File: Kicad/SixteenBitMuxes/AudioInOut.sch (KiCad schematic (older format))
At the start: 3 parts, among them J1 Audio In/Out JST XH, U25 CD4053B

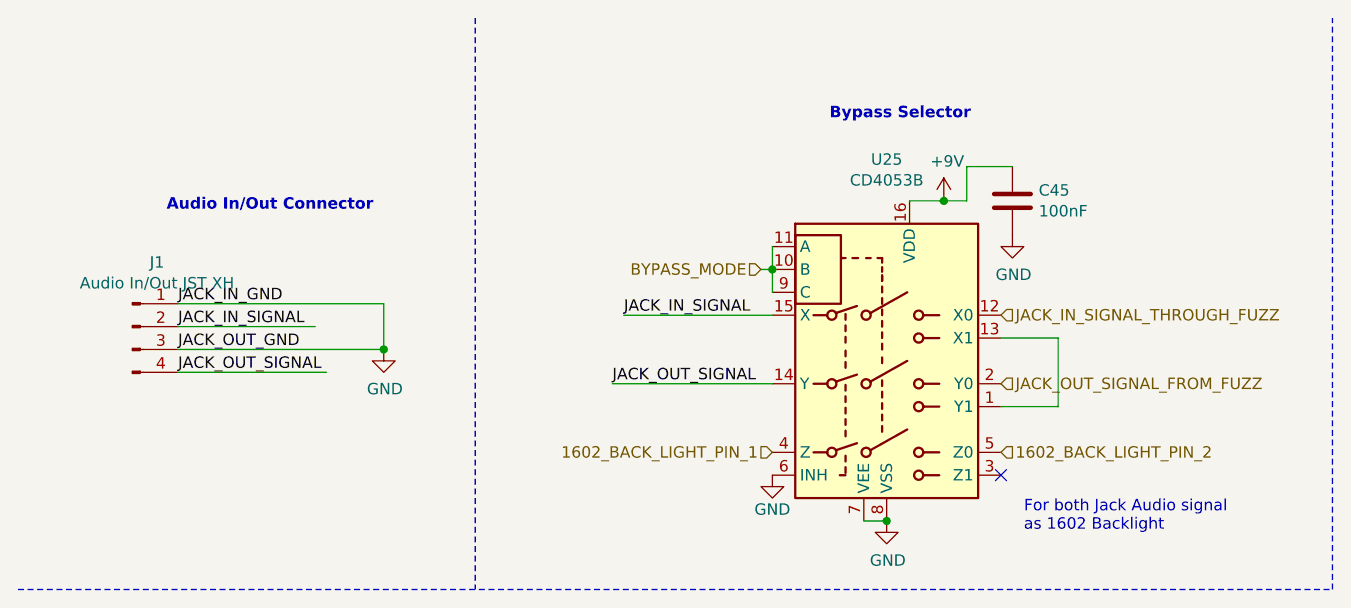
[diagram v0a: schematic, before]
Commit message: LCD backlight and backlight removed from circuit/pcb.
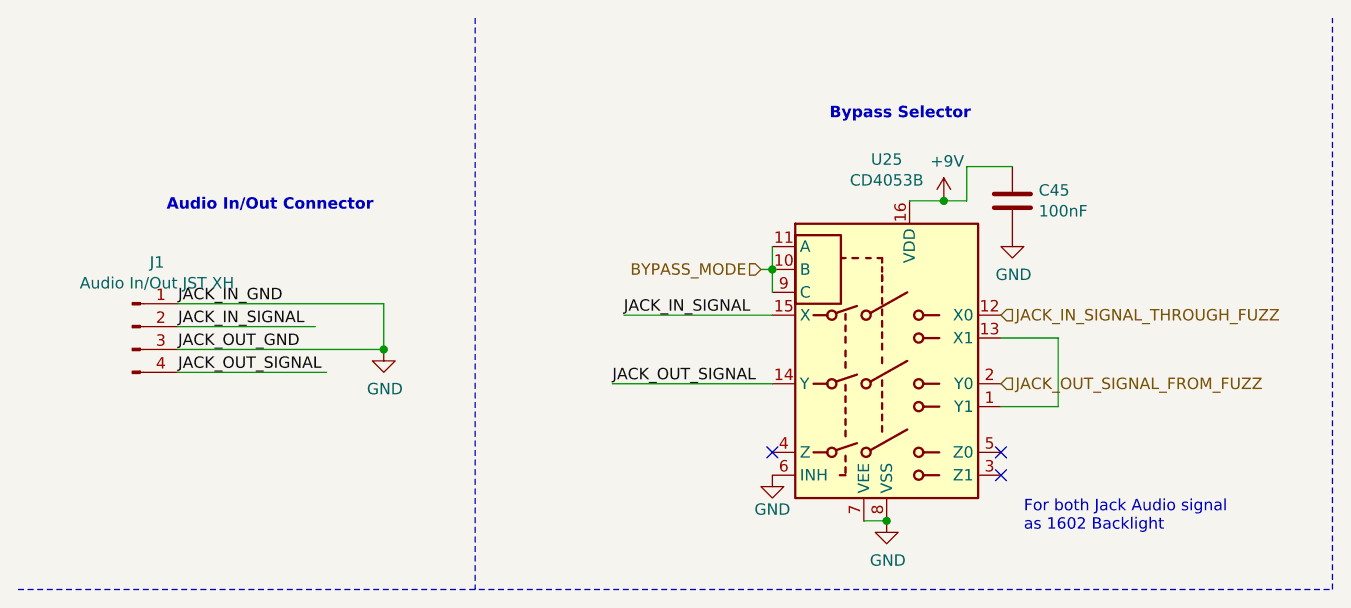
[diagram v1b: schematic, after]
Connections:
- net labels removed: 1602_BACK_LIGHT_PIN_1, 1602_BACK_LIGHT_PIN_2
- no-connect marks 1 -> 3
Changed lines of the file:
@@
 	4250 2700 4350 2700
 Connection ~ 4350 2700
-Text HLabel 3850 2400 0    50   Input ~ 0
-1602_BACK_LIGHT_PIN_1
-Text HLabel 4850 2400 2    50   Input ~ 0
-1602_BACK_LIGHT_PIN_2
 NoConn ~ 4850 2500
 Text Notes 4950 2750 0    50   ~ 0
@@
 Wire Notes Line
 	550  3000 6300 3000
+NoConn ~ 4850 2400
+NoConn ~ 3850 2400
 $EndSCHEMATC

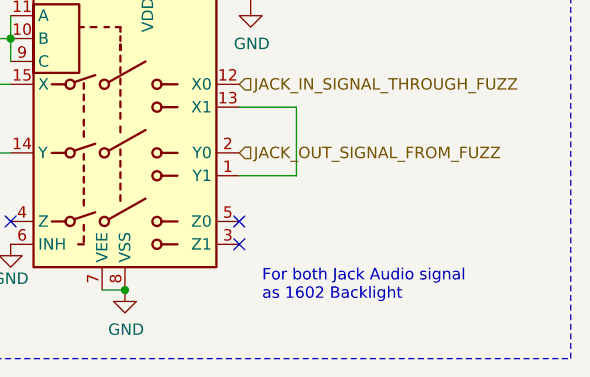
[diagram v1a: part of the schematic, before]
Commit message: PCB Logo/texts
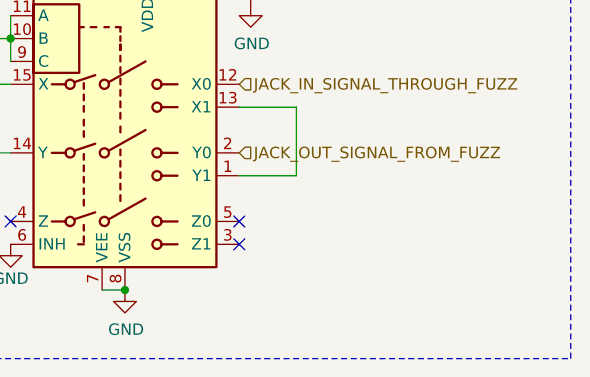
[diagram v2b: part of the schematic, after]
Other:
- note added: "\n"
- note removed: "For both Jack Audio signal \nas 1602 Backlight"
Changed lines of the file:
@@
 NoConn ~ 4850 2500
 Text Notes 4950 2750 0    50   ~ 0
-For both Jack Audio signal \nas 1602 Backlight
+\n
 Wire Notes Line
 	550  3000 6300 3000

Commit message: PCB mostly
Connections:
- net labels added: GNDA
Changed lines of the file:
@@
 Text Label 1250 2050 0    50   ~ 0
 JACK_OUT_SIGNAL
-$Comp
-L power:GND #PWR?
-U 1 1 5EDE8C24
-P 2150 1950
-AR Path="/5EDE8C24" Ref="#PWR?"  Part="1"
-AR Path="/5EDE1E76/5EDE8C24" Ref="#PWR06"  Part="1"
-F 0 "#PWR06" H 2150 1700 50  0001 C CNN
-F 1 "GND" H 2155 1777 50  0000 C CNN
-F 2 "" H 2150 1950 50  0001 C CNN
-F 3 "" H 2150 1950 50  0001 C CNN
-	1    2150 1950
-	1    0    0    -1
-$EndComp
 Wire Wire Line
 	1250 1950 2150 1950
 Wire Wire Line
 	2150 1750 2150 1950
-Connection ~ 2150 1950
 Wire Wire Line
 	1250 1750 2150 1750
@@
 NoConn ~ 4850 2400
 NoConn ~ 3850 2400
+$Comp
+L power:GNDA #PWR0116
+U 1 1 5EDAFA9A
+P 2150 1950
+F 0 "#PWR0116" H 2150 1700 50  0001 C CNN
+F 1 "GNDA" H 2155 1777 50  0000 C CNN
+F 2 "" H 2150 1950 50  0001 C CNN
+F 3 "" H 2150 1950 50  0001 C CNN
+	1    2150 1950
+	1    0    0    -1
+$EndComp
+Connection ~ 2150 1950
 $EndSCHEMATC

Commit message: Improvements according video youtube
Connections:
- net labels added: +9V_SAFE
- net labels removed: +9V
- wire segments 18 -> 16
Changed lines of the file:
@@
 Text Label 3150 2100 0    50   ~ 0
 JACK_OUT_SIGNAL
-Text Notes 4100 950  0    50   ~ 10
+Text Notes 3800 750  0    50   ~ 10
 Bypass Selector
 Text Notes 1200 1350 0    50   ~ 10
@@
 	1    0    0    -1
 $EndComp
-Wire Wire Line
-	4700 1300 4700 1150
-Wire Wire Line
-	4700 1150 4900 1150
-$Comp
-L power:+9V #PWR?
-U 1 1 5E94F0DF
-P 4600 1300
-AR Path="/5E9AE796/5E94F0DF" Ref="#PWR?"  Part="1"
-AR Path="/5F9746B8/5E94F0DF" Ref="#PWR?"  Part="1"
-AR Path="/5EDE1E76/5E94F0DF" Ref="#PWR08"  Part="1"
-F 0 "#PWR08" H 4600 1150 50  0001 C CNN
-F 1 "+9V" H 4615 1473 50  0000 C CNN
-F 2 "" H 4600 1300 50  0001 C CNN
-F 3 "" H 4600 1300 50  0001 C CNN
-	1    4600 1300
-	1    0    0    -1
-$EndComp
-Connection ~ 4600 1300
-Wire Wire Line
-	4600 1300 4700 1300
 Text HLabel 3800 1600 0    50   Input ~ 0
 BYPASS_MODE
@@
 Text HLabel 4850 2100 2    50   Input ~ 0
 JACK_OUT_SIGNAL_FROM_FUZZ
-Wire Wire Line
-	4450 1300 4600 1300
 Wire Wire Line
 	3850 1800 3200 1800
@@
 U 1 1 5E949734
 P 4350 2000
-F 0 "U25" H 4350 2881 50  0000 C CNN
-F 1 "CD4053B" H 4350 2790 50  0000 C CNN
+F 0 "U25" H 4050 2800 50  0000 C CNN
+F 1 "CD4053B" H 4050 2700 50  0000 C CNN
 F 2 "Package_SO:SOIC-16_3.9x9.9mm_P1.27mm" H 4500 1250 50  0001 L CNN
 F 3 "http://www.ti.com/lit/ds/symlink/cd4052b.pdf" H 4330 2200 50  0001 C CNN
@@
 $EndComp
 Connection ~ 2150 1950
+Text HLabel 4700 1150 1    50   Input ~ 0
++9V_SAFE
+Wire Wire Line
+	4450 1150 4900 1150
+Wire Wire Line
+	4450 1150 4450 1300
 $EndSCHEMATC

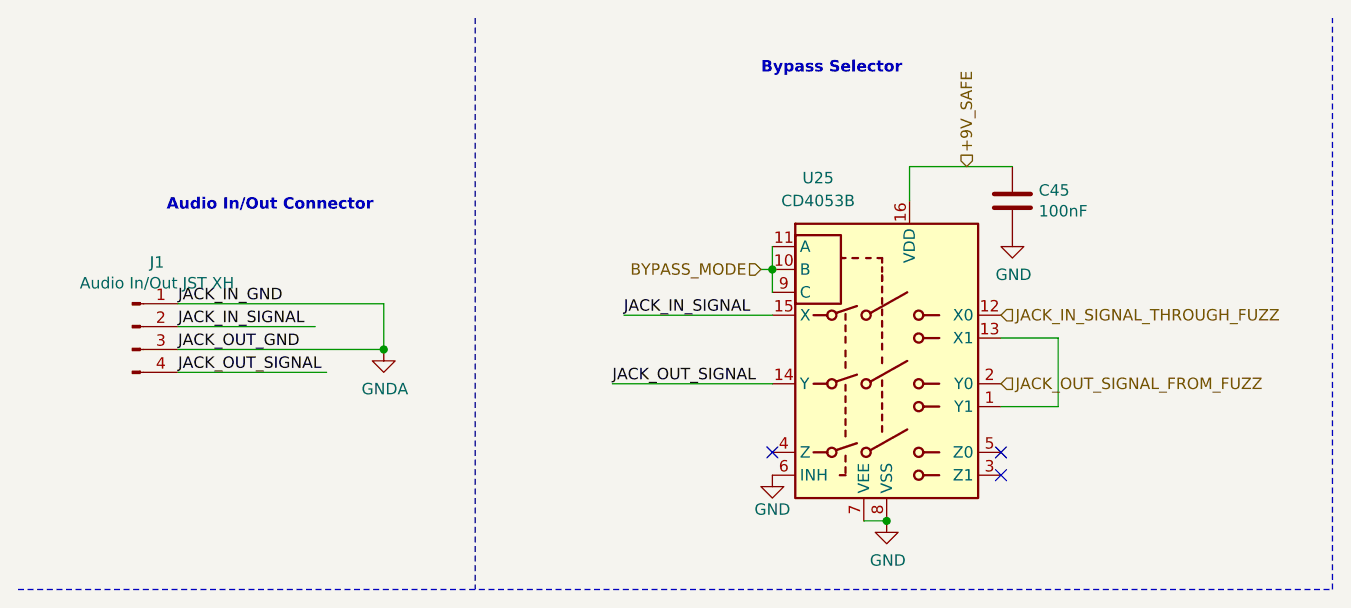
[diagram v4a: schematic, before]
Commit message: UART, BOOT, NRST, Isolated OSC gnd
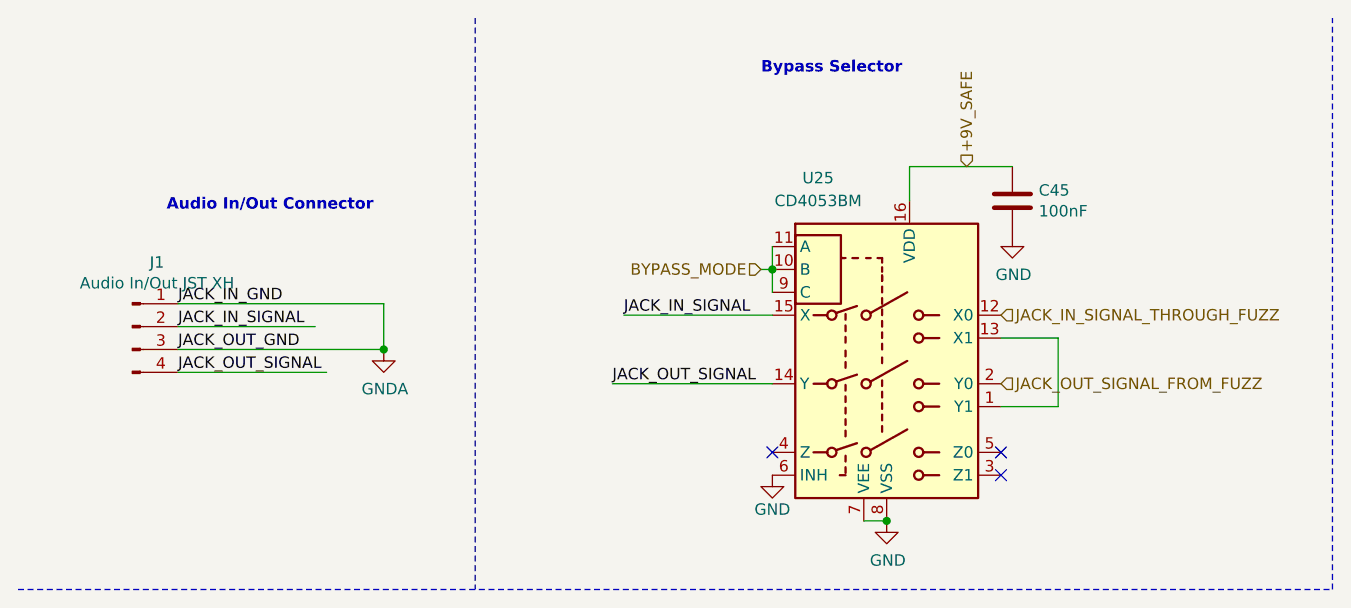
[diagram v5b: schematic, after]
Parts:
- U25: value CD4053B -> CD4053BM
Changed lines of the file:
@@
 P 4350 2000
 F 0 "U25" H 4050 2800 50  0000 C CNN
-F 1 "CD4053B" H 4050 2700 50  0000 C CNN
+F 1 "CD4053BM" H 4050 2700 50  0000 C CNN
 F 2 "Package_SO:SOIC-16_3.9x9.9mm_P1.27mm" H 4500 1250 50  0001 L CNN
 F 3 "http://www.ti.com/lit/ds/symlink/cd4052b.pdf" H 4330 2200 50  0001 C CNN
